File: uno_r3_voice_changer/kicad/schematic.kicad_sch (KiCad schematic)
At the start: 11 parts, among them SW1 FX, SW2 PARAM

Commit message: Refactor code structure for improved readability and maintainability
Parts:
- R1, R2: value 10k -> 100k
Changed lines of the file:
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@@
 			)
 		)
-		(property "Value" "10k"
+		(property "Value" "100k"
 			(at 80.01 66.0399 0)
 			(effects
@@
 			)
 		)
-		(property "Value" "10k"
+		(property "Value" "100k"
 			(at 80.01 53.3399 0)
 			(effects

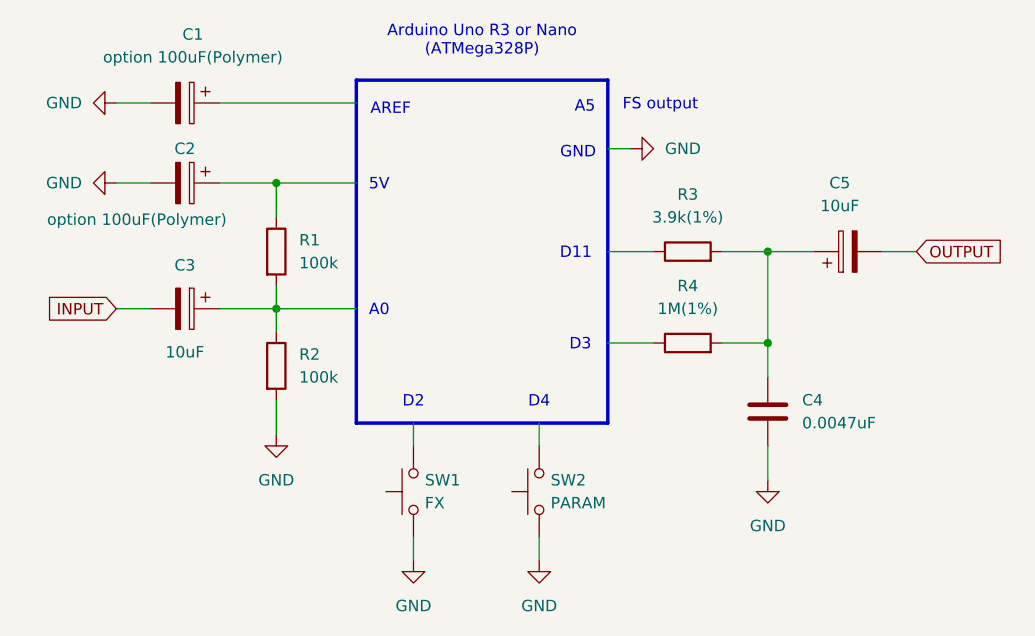
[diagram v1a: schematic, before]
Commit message: Update schematic image for Uno R3 Voice Changer
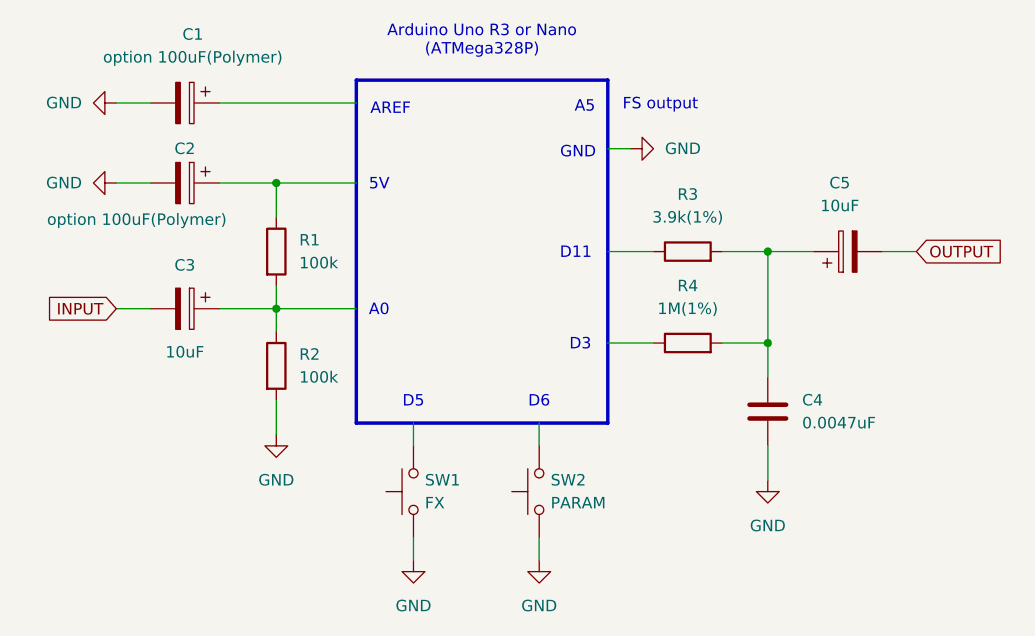
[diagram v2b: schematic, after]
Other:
- note added: "D5"
- note added: "D6"
- note removed: "D2"
- note removed: "D4"
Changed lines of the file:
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@@
 		)
 	)
-	(text "D2"
+	(text "D5"
 		(exclude_from_sim no)
 		(at 92.71 68.834 0)
@@
 		)
 	)
-	(text "D4"
+	(text "D6"
 		(exclude_from_sim no)
 		(at 106.68 68.834 0)
